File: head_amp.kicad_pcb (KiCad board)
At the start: 4 copper layers, 50 x 50 mm, 53 parts, among them J1 Conn_01x15, J2 Conn_01x15, J3 Conn_01x05, J4 Conn_01x03, J5 Left_Speaker, J6 Left_Speaker, J7 Left_Speaker, J8 Left_Speaker, M1 Fan, Q1 AO3401A, Q2 AO3400A, U2 Headphone Jack, U3 WM8988LGECN/V, U4 WM8988LGECN/V

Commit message: feat: overhaul
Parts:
- removed C11: 4.7u, Capacitor_SMD:C_0603_1608Metric
- removed H2, H3, H4: MountingHole, MountingHole:MountingHole_2.2mm_M2
- removed M1: Fan, A2543WR-4P:MOLEX_22053041
- removed NT1: NetTie_2, NetTie:NetTie-2_THT_Pad1.0mm
- removed U3: WM8988LGECN/V, footprints:QFN28_4X4_CIR
- added C2: 100n, Capacitor_SMD:C_0603_1608Metric, F.Cu at (130.8, 110.0)
- added C3: 22u, Capacitor_SMD:C_0603_1608Metric, F.Cu at (133.2, 110.5)
- added C30: 100u, Capacitor_SMD:C_1206_3216Metric, F.Cu at (137.0, 80.5)
- added C31: 100u, Capacitor_SMD:C_1206_3216Metric, F.Cu at (137.0, 78.0)
- added C32: 4.7u, Capacitor_SMD:C_0402_1005Metric, F.Cu at (134.5, 84.5)
- added C33: 4.7u, Capacitor_SMD:C_0402_1005Metric, F.Cu at (135.5, 84.5)
- added C34: 1u, Capacitor_SMD:C_0402_1005Metric, F.Cu at (132.5, 89.0)
- added C35: 4.7u, Capacitor_SMD:C_0402_1005Metric, F.Cu at (137.5, 84.5)
- added C36: 4.7u, Capacitor_SMD:C_0402_1005Metric, F.Cu at (136.5, 84.5)
- added C37: 1u, Capacitor_SMD:C_0402_1005Metric, F.Cu at (132.5, 82.5)
- added C38: 100n, Capacitor_SMD:C_0603_1608Metric, F.Cu at (159.5, 101.3)
- added C39: 10u, Capacitor_SMD:C_0603_1608Metric, F.Cu at (133.2, 106.2)
- added C40: 22u, Capacitor_SMD:C_0603_1608Metric, F.Cu at (133.2, 103.2)
- added Q3: AO3401A, Package_TO_SOT_SMD:SOT-23, F.Cu at (162.0, 103.1)
- added Q4: AO3400A, Package_TO_SOT_SMD:SOT-23, F.Cu at (162.0, 98.9)
- added R10: 10k, Resistor_SMD:R_0402_1005Metric, F.Cu at (132.5, 80.5)
- added R13: 10k, Resistor_SMD:R_0402_1005Metric, F.Cu at (165.0, 121.5)
- added R14: 10k, Resistor_SMD:R_0402_1005Metric, F.Cu at (144.5, 104.0)
- added R6: 10k, Resistor_SMD:R_0402_1005Metric, F.Cu at (137.5, 124.4)
- added R8: 10k, Resistor_SMD:R_0402_1005Metric, F.Cu at (132.5, 91.0)
- added R9: 10k, Resistor_SMD:R_0402_1005Metric, F.Cu at (144.0, 88.5)
- added SW1: SW_Push, Button_Switch_SMD:SW_SPST_TS-1088-xR020, F.Cu at (166.5, 114.5)
- added SW2: SW_Push, Button_Switch_SMD:SW_SPST_TS-1088-xR020, F.Cu at (166.5, 118.0)
- added U1: AMS1117-3.3, Package_TO_SOT_SMD:SOT-223-3_TabPin2, F.Cu at (138.7, 112.0)
- added U5: WM8988LGECN/V, footprints:QFN28_4X4_CIR, F.Cu at (157.6, 88.3)
- added U6: WM8988LGECN/V, footprints:QFN28_4X4_CIR, F.Cu at (136.6, 88.3)
- added U7: AMS1117-3.3, Package_TO_SOT_SMD:SOT-223-3_TabPin2, F.Cu at (138.7, 104.7)
- added U8: ESP32-WROOM-32E, RF_Module:ESP32-WROOM-32E, F.Cu at (153.2, 118.9)
- C1: value 100n -> 10u
- C10: value 100u -> 1u; footprint Capacitor_SMD:C_1206_3216Metric -> Capacitor_SMD:C_0603_1608Metric
- C12, C15, C25, C28, C8: value 4.7u -> 100n; footprint Capacitor_SMD:C_0603_1608Metric -> Capacitor_SMD:C_0402_1005Metric
- C13, C26: value 1u -> 100u; footprint Capacitor_SMD:C_0603_1608Metric -> Capacitor_SMD:C_1206_3216Metric
- C14, C27: value 4.7u -> 100u; footprint Capacitor_SMD:C_0603_1608Metric -> Capacitor_SMD:C_1206_3216Metric
- C16, C29: value 1u -> 4.7u; footprint Capacitor_SMD:C_0603_1608Metric -> Capacitor_SMD:C_0402_1005Metric
- C17: value 100n -> 100u; footprint Capacitor_SMD:C_0603_1608Metric -> Capacitor_SMD:C_1206_3216Metric
- C19, C22, C23: value 100u -> 4.7u; footprint Capacitor_SMD:C_1206_3216Metric -> Capacitor_SMD:C_0402_1005Metric
- C20: value 100n -> 4.7u; footprint Capacitor_SMD:C_0603_1608Metric -> Capacitor_SMD:C_0402_1005Metric
- C21, C24: value 4.7u -> 1u; footprint Capacitor_SMD:C_0603_1608Metric -> Capacitor_SMD:C_0402_1005Metric
- C5, C6: value 100u -> 100n; footprint Capacitor_SMD:C_1206_3216Metric -> Capacitor_SMD:C_0402_1005Metric
- C7: footprint Capacitor_SMD:C_0603_1608Metric -> Capacitor_SMD:C_0402_1005Metric
- C9: value 100u -> 100n; footprint Capacitor_SMD:C_1206_3216Metric -> Capacitor_SMD:C_0603_1608Metric
- H1: footprint MountingHole:MountingHole_2.2mm_M2 -> MountingHole:MountingHole_3.2mm_M3
- J1: value Conn_01x15 -> USB Port; footprint Connector_PinHeader_2.54mm:PinHeader_1x15_P2.54mm_Vertical -> Connector_USB:USB_C_Receptacle_GCT_USB4105-xx-A_16P_TopMnt_Horizontal
- J2: value Conn_01x15 -> I2C; footprint Connector_PinHeader_2.54mm:PinHeader_1x15_P2.54mm_Vertical -> Connector_JST:JST_EH_S5B-EH_1x05_P2.50mm_Horizontal
- J3: value Conn_01x05 -> LED; footprint Connector_JST:JST_EH_S5B-EH_1x05_P2.50mm_Horizontal -> Connector_JST:JST_EH_S3B-EH_1x03_P2.50mm_Horizontal
- J4: value Conn_01x03 -> Left_Mic; footprint Connector_JST:JST_EH_S3B-EH_1x03_P2.50mm_Horizontal -> Connector_JST:JST_EH_S2B-EH_1x02_P2.50mm_Horizontal
- J6: value Left_Speaker -> Right_Mic
- J7: value Left_Speaker -> Right_Speaker
- J8: value Left_Speaker -> Fan
- NT2: footprint NetTie:NetTie-2_THT_Pad1.0mm -> NetTie:NetTie-2_SMD_Pad2.0mm; moved to B.Cu
- Q1: value AO3401A -> MMBT3904
- Q2: value AO3400A -> MMBT3904
- R1: value 50k -> 22; footprint Resistor_SMD:R_0603_1608Metric -> Resistor_SMD:R_0402_1005Metric
- R2: value 27k -> 22; footprint Resistor_SMD:R_0603_1608Metric -> Resistor_SMD:R_0402_1005Metric
- R3, R4: value 10k -> 5.1k; footprint Resistor_SMD:R_0603_1608Metric -> Resistor_SMD:R_0402_1005Metric
- R5: footprint Resistor_SMD:R_0603_1608Metric -> Resistor_SMD:R_0402_1005Metric
- U2: value Headphone Jack -> CH340K; footprint PJ-320A:PJ-320A -> Package_SO:SSOP-10-1EP_3.9x4.9mm_P1mm_EP2.1x3.3mm
- U4: value WM8988LGECN/V -> Headphone Jack; footprint footprints:QFN28_4X4_CIR -> PJ-320A:PJ-320A
- moved C9 52.5 mm to (164.0, 123.6), turned to 90 degrees
- moved C10 51.3 mm to (165.5, 123.6), turned to -90 degrees
- moved C13 43.0 mm to (159.0, 78.0), turned to 180 degrees
- moved C5 42.7 mm to (142.5, 120.5), turned to 90 degrees
- moved R4 41.6 mm to (133.0, 120.0), turned to 0 degrees
- moved C6 41.3 mm to (142.5, 116.5), turned to 90 degrees
- moved C22 40.7 mm to (158.5, 84.5), turned to -90 degrees
- moved C23 37.9 mm to (157.5, 84.5), turned to -90 degrees
- moved C16 37.6 mm to (161.0, 89.0), turned to 0 degrees
- moved C18 36.6 mm to (154.0, 78.0), turned to 180 degrees
- moved J2 36.6 mm to (130.0, 106.0), turned to 90 degrees
- moved J5 35.7 mm to (166.0, 78.8), turned to -90 degrees
- moved C19 34.5 mm to (155.5, 84.5), turned to -90 degrees
- moved J1 33.5 mm to (127.0, 118.5), turned to -90 degrees
- moved R3 31.0 mm to (133.0, 117.0), turned to 0 degrees
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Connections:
- C1 pad 1: +5V -> GND
- C1 pad 2: GND -> +5V
- C10 pad 1: /Speaker_Left -> +3V3D
- C10 pad 2: Net-(U3-LOUT1) -> GND
- C12 pad 2: Net-(U3-VREF) -> +3V3D
- C13 pad 1: /Headset_Mic -> /Speaker_Right
- C13 pad 2: Net-(U3-LINPUT1) -> Net-(U5-ROUT1)
- C14 pad 1: GNDA -> /Speaker_Right
- C14 pad 2: +3V3A -> Net-(U5-ROUT1)
- C15 pad 1: GNDA -> GND
- C15 pad 2: +3V3A -> +3V3D
- C16 pad 1: /Headset_Mic -> Net-(U5-HPCOM)
- C16 pad 2: Net-(U3-RINPUT1) -> GNDA
- C17 pad 1: GND -> /Speaker_Left
- C17 pad 2: +3V3D -> Net-(U5-LOUT1)
- C18 pad 1: /Headset_Right -> /Speaker_Left
- C18 pad 2: Net-(U4-ROUT1) -> Net-(U5-LOUT1)
- C19 pad 1: /Headset_Right -> GND
- C19 pad 2: Net-(U4-ROUT1) -> Net-(U5-VMID)
- C20 pad 2: +3V3D -> Net-(U5-VREF)
- C21 pad 1: Net-(U4-HPCOM) -> /Headset_Mic
- C21 pad 2: GNDA -> Net-(U5-LINPUT1)
- C22 pad 1: /Headset_Left -> GNDA
- C22 pad 2: Net-(U4-LOUT1) -> +3V3A
- C23 pad 1: /Headset_Left -> GNDA
- C23 pad 2: Net-(U4-LOUT1) -> +3V3A
- C24 pad 1: GND -> /Headset_Mic
- C24 pad 2: Net-(U4-VMID) -> Net-(U5-RINPUT1)
- C25 pad 2: Net-(U4-VREF) -> +3V3D
- C26 pad 1: /Mic_Left -> /Headset_Right
- C26 pad 2: Net-(U4-LINPUT1) -> Net-(U6-ROUT1)
- C27 pad 1: GNDA -> /Headset_Right
- C27 pad 2: +3V3A -> Net-(U6-ROUT1)
- C28 pad 1: GNDA -> GND
- C28 pad 2: +3V3A -> +3V3D
- C29 pad 1: /Mic_Right -> Net-(U6-HPCOM)
- C29 pad 2: Net-(U4-RINPUT1) -> GNDA
- C4 pad 1: GND -> +5V
- C4 pad 2: +3V3D -> GND
- C5 pad 1: /Speaker_Right -> GND
- C5 pad 2: Net-(U3-ROUT1) -> +3V3D
- C6 pad 1: /Speaker_Right -> Net-(U2-V3)
- C6 pad 2: Net-(U3-ROUT1) -> GND
- C7 pad 2: +3V3D -> /GPIO0
- C8 pad 1: Net-(U3-HPCOM) -> GND
- C8 pad 2: GNDA -> /MCU_EN
- C9 pad 1: /Speaker_Left -> GND
- C9 pad 2: Net-(U3-LOUT1) -> +3V3D
- J2 pad 1: unconnected-(J2-Pin_1-Pad1) -> +5V
- J2 pad 2: unconnected-(J2-Pin_2-Pad2) -> +3V3D
- J2 pad 5: /Int->Ext_Out -> GND
- J3 pad 2: +3V3D -> /LED_Data
- J3 pad 3: /Out_DAT -> GND
- J4 pad 1: +5V -> /Mic_Left
- J4 pad 2: /LED_Data -> GNDA
- J6 pad 1: /Mic_Left -> /Mic_Right
- J8 pad 1: /Mic_Right -> Net-(J8-Pin_1)
- J8 pad 2: GNDA -> GND
- Q1 pad 1: /FAN_PWM -> Net-(Q1-B)
- Q1 pad 2: +5V -> /RTS
- Q1 pad 3: Net-(M1-PWM) -> /MCU_EN
- Q2 pad 1: /FAN_PWM -> Net-(Q2-B)
- Q2 pad 2: GND -> /DTR
- Q2 pad 3: Net-(M1-PWM) -> /GPIO0
- R1 pad 1: GND -> Net-(J1-D--PadA7)
- R1 pad 2: /FAN_RPM -> /USB_D-
- R2 pad 1: /FAN_RPM -> Net-(J1-D+-PadA6)
- R2 pad 2: Net-(M1-Tacho) -> /USB_D+
- R3 pad 1: /Mic_Left -> Net-(J1-CC1)
- R3 pad 2: +3V3A -> GND
- R4 pad 1: /Mic_Right -> Net-(J1-CC2)
- R4 pad 2: +3V3A -> GND
- R5 pad 1: +3V3A -> /DTR
- R5 pad 2: /Headset_Mic -> Net-(Q1-B)
- U2 pad 1: /Headset_Mic -> /USB_D+
- U2 pad 2: /Headset_Left -> /USB_D-
- U2 pad 3: /Headset_Right -> GND
- U2 pad 4: GNDA -> /DTR
- U4 pad 1: /Master_Audio_Clk -> /Headset_Mic
- U4 pad 2: +3V3D -> /Headset_Left
- U4 pad 3: +3V3D -> /Headset_Right
- U4 pad 4: GND -> GNDA
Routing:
- net /GPIO0: track 0.00 -> 128.6 mm, vias 0 -> 9
- net GND: track 25.2 -> 102.6 mm, vias 6 -> 14
- net /SPI_CLK: track 23.6 -> 67.6 mm, vias 2 -> 3
- net /MOSI: track 22.7 -> 64.9 mm, vias 2 -> 3
- net GNDA: track 56.6 -> 15.3 mm, vias 2 -> 6
- net Net-(U3-LOUT1): track 37.2 -> 0.00 mm, vias 2 -> 0
- net /MCU_EN: track 0.00 -> 34.0 mm
- net /Ext->Int_Select: track 0.00 -> 30.7 mm, vias 0 -> 2
- net Net-(U3-LINPUT1): track 26.3 -> 0.00 mm, vias 2 -> 0
- net /Master_Audio_Clk: track 25.9 -> 0.00 mm, vias 2 -> 0
- net Net-(U3-RINPUT1): track 25.8 -> 0.00 mm, vias 2 -> 0
- net /Fan_PWM: track 0.00 -> 25.2 mm
- net Net-(U3-ROUT1): track 23.3 -> 0.00 mm, vias 2 -> 0
- net Net-(U4-LOUT1): track 23.3 -> 0.00 mm, vias 2 -> 0
- net +5V: track 8.54 -> 29.9 mm, vias 1 -> 3
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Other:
- board text added: "Boot"
- board text added: "En"
- board text added: "Fan"
- board text added: "I2C"
- board text added: "LED"
- board text added: "Left"
- board text added: "Microphone"
- board text added: "Right"
- board text added: "Speaker"

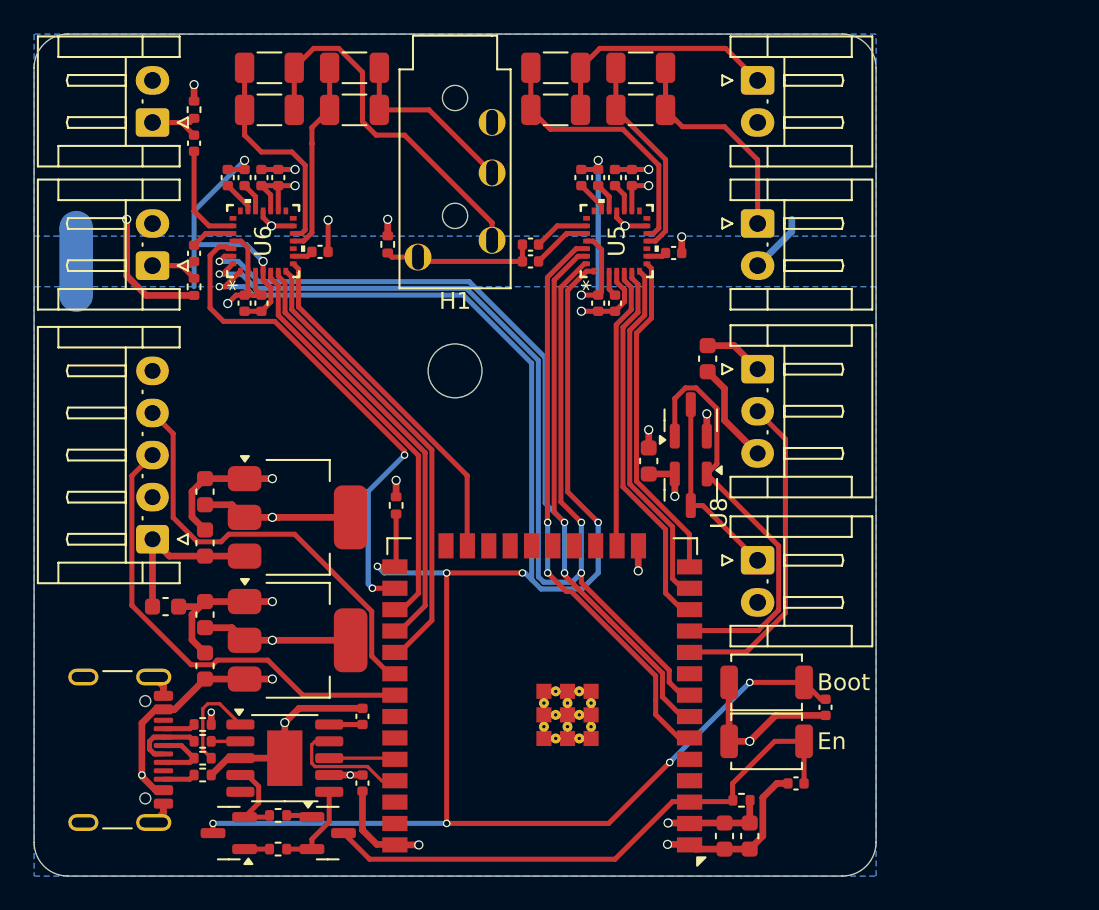
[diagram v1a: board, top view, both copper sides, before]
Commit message: add 3d models and tooling holes
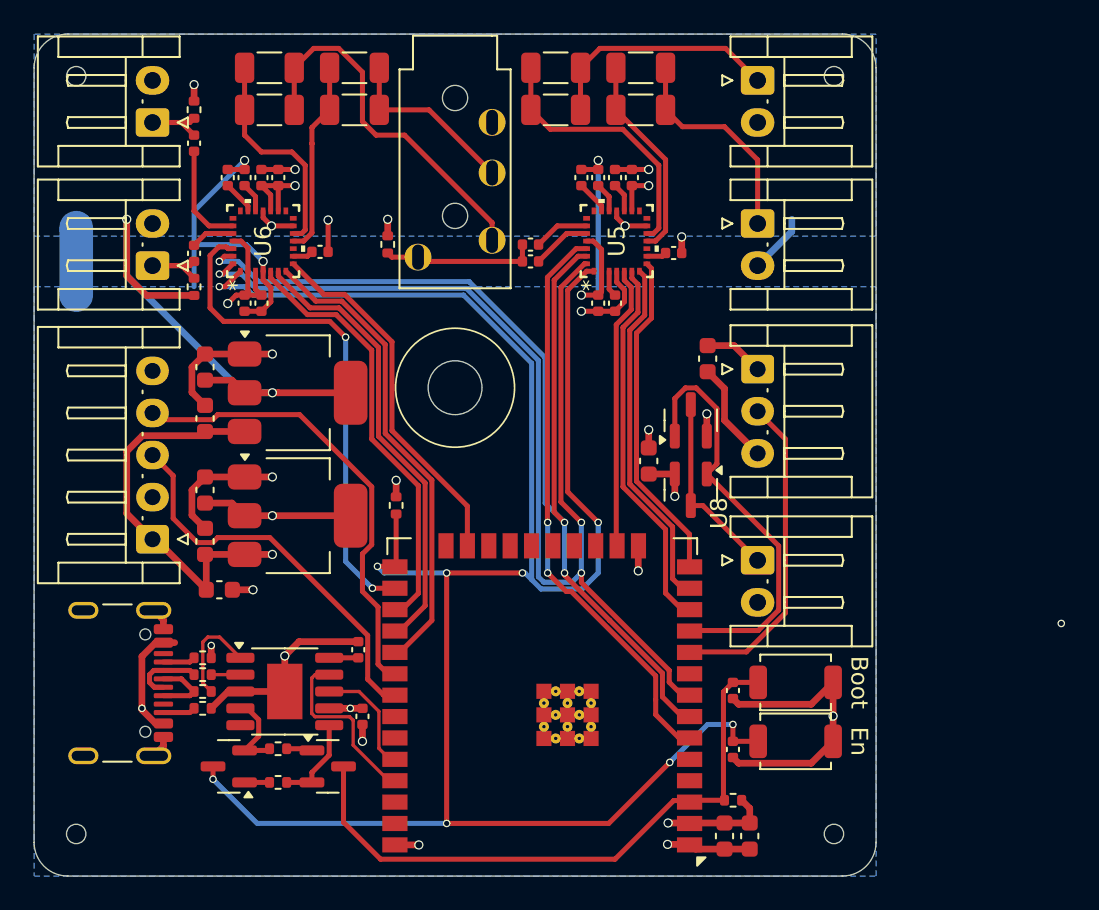
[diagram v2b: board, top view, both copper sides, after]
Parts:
- added H2: ToolingHole, MountingHole:ToolingHole_1.152mm, F.Cu at (125.5, 78.5)
- added H3: ToolingHole, MountingHole:ToolingHole_1.152mm, F.Cu at (170.5, 123.5)
- added H4: ToolingHole, MountingHole:ToolingHole_1.152mm, F.Cu at (125.5, 123.5)
- added H5: ToolingHole, MountingHole:ToolingHole_1.152mm, F.Cu at (170.5, 78.5)
- moved C1 7.40 mm to (133.2, 106.1)
- moved U1 7.40 mm to (138.7, 104.6)
- moved U7 7.40 mm to (138.7, 97.3)
- moved C3 7.40 mm to (133.2, 103.1)
- moved C39 7.40 mm to (133.2, 98.8)
- moved C40 7.40 mm to (133.2, 95.8)
- moved C8 6.67 mm to (164.5, 115.0), turned to 90 degrees
- moved C7 6.04 mm to (164.5, 118.5)
- moved C6 3.97 mm to (142.2, 112.6)
- moved C5 3.96 mm to (142.5, 116.5)
- moved Q1 3.96 mm to (140.4, 119.5)
- moved Q2 3.96 mm to (134.6, 119.5)
- moved R5 3.96 mm to (137.5, 118.4)
- moved R6 3.96 mm to (137.5, 120.4)
- moved J1 3.96 mm to (127.0, 114.5)
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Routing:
- net +5V: track 29.9 -> 37.4 mm
- net +3V3A: track 49.5 -> 43.1 mm
- net /Out_DAT: track 27.5 -> 23.6 mm
- net /GPIO0: track 128.6 -> 125.4 mm
- net /MCU_EN: track 34.0 -> 37.1 mm
- net /Prog_TX: track 7.88 -> 11.0 mm
- net /Prog_RX: track 3.98 -> 7.02 mm
- net GND: track 102.6 -> 100.3 mm, vias 14 -> 16
- net /Out_CLK: track 26.1 -> 27.9 mm
- net /Ext->Int_In: track 25.9 -> 26.9 mm
- net /Ext->Int_CLK: track 24.6 -> 25.6 mm
- net /Ext->Int_LRC: track 27.3 -> 28.2 mm
- net /Ext->Int_Out: track 21.0 -> 21.8 mm
- net (no net): vias 0 -> 1

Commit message: compactify
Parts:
- added H6: MountingHole, MountingHole:MountingHole_3.2mm_M3, F.Cu at (136.0, 122.5)
- C4: footprint Capacitor_SMD:C_0603_1608Metric -> Capacitor_SMD:C_0402_1005Metric
- moved J8 11.5 mm to (166.0, 95.8)
- moved C4 9.47 mm to (163.5, 104.7)
- moved C10 9.03 mm to (164.0, 114.7), turned to 90 degrees
- moved J3 8.35 mm to (166.0, 104.2)
- moved R13 6.07 mm to (165.5, 115.5), turned to -90 degrees
- moved U8 5.64 mm to (153.2, 113.2)
- moved R14 5.64 mm to (144.5, 98.3)
- moved C38 5.63 mm to (159.6, 95.7)
- moved Q3 5.63 mm to (162.1, 97.4)
- moved Q4 5.63 mm to (162.1, 93.3)
- moved C9 5.62 mm to (164.0, 118.0)
- moved H1 2.83 mm to (150.0, 95.0)
- moved C6 2.10 mm to (142.8, 110.5)
- moved U2 2.09 mm to (138.4, 113.0)
- moved Q1 2.09 mm to (140.9, 117.5)
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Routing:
- net /GPIO0: track 125.4 -> 106.0 mm, vias 9 -> 8
- net /LED_Data: track 19.2 -> 4.18 mm
- net /SPI_CLK: track 67.6 -> 56.9 mm
- net /MOSI: track 64.9 -> 54.2 mm
- net /MCU_EN: track 37.1 -> 29.7 mm
- net /Out_CLK: track 27.9 -> 21.7 mm
- net /Ext->Int_Select: track 30.9 -> 24.7 mm, vias 2 -> 0
- net /Ext->Int_CLK: track 25.6 -> 19.6 mm
- net /Ext->Int_LRC: track 28.2 -> 22.3 mm
- net /Ext->Int_In: track 26.9 -> 21.1 mm
- net /Int->Ext_In: track 22.5 -> 16.8 mm
- net /Ext->Int_Out: track 21.8 -> 16.1 mm
- net /Int->Ext_Select: track 34.4 -> 28.8 mm
- net /Int->Ext_Out: track 19.8 -> 14.1 mm
- net /Int->Ext_LRC: track 21.1 -> 15.4 mm
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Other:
- board text removed: "Boot"
- board text removed: "En"
